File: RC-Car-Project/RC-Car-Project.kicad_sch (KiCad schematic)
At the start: 4 parts

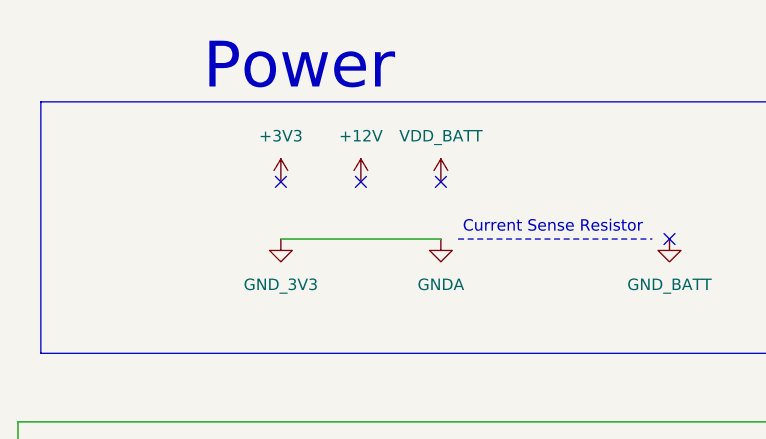
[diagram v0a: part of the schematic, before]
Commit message: Added Camera Connector, Minor Controller Fixes
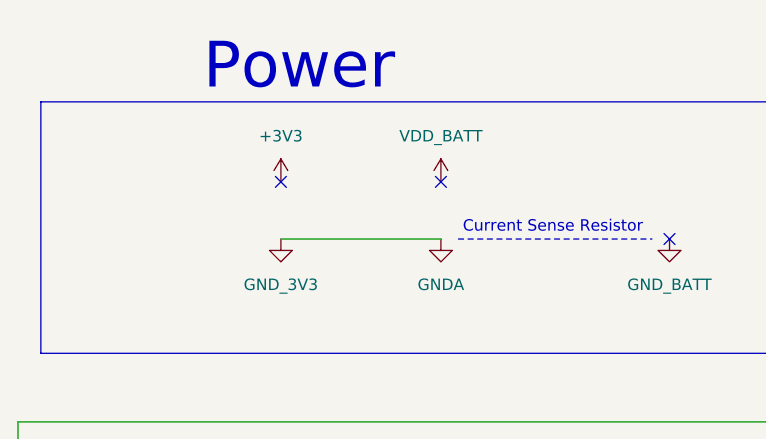
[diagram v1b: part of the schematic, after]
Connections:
- no-connect marks 5 -> 4
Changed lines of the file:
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@@
-	)
-	(no_connect
-		(at 81.28 34.29)
 	)
 	(no_connect
@@
 					(unit 1)
 				)
-			)
-		)
-	)
-	(symbol
-		(lib_id "power:+3V3")
-		(at 81.28 34.29 0)
-		(unit 1)
-		(exclude_from_sim no)
-		(in_bom yes)
-		(on_board yes)
-		(dnp no)
-		(fields_autoplaced yes)
-		(property "Reference" "#PWR012"
-			(at 81.28 38.1 0)
-			(effects
-				(font
-					(size 1.27 1.27)
-				)
-				(hide yes)
-			)
-		)
-		(property "Value" "+12V"
-			(at 81.28 29.21 0)
-			(effects
-				(font
-					(size 1.27 1.27)
-				)
-			)
-		)
-		(property "Footprint" ""
-			(at 81.28 34.29 0)
-			(effects
-				(font
-					(size 1.27 1.27)
-				)
-				(hide yes)
-			)
-		)
-		(property "Datasheet" ""
-			(at 81.28 34.29 0)
-			(effects
-				(font
-					(size 1.27 1.27)
-				)
-				(hide yes)
-			)
-		)
-		(property "Description" "Power symbol creates a global label with name \"+3V3\""
-			(at 81.28 34.29 0)
-			(effects
-				(font
-					(size 1.27 1.27)
-				)
-				(hide yes)
-			)
-		)
-		(pin "1"
-		)
-		(instances
-			(project "RC-Car-Project"
-				(path "/ba870fd1-751d-4755-8e1a-1ea86ca9e2f6"
-					(reference "#PWR012")
-					(unit 1)
-				)

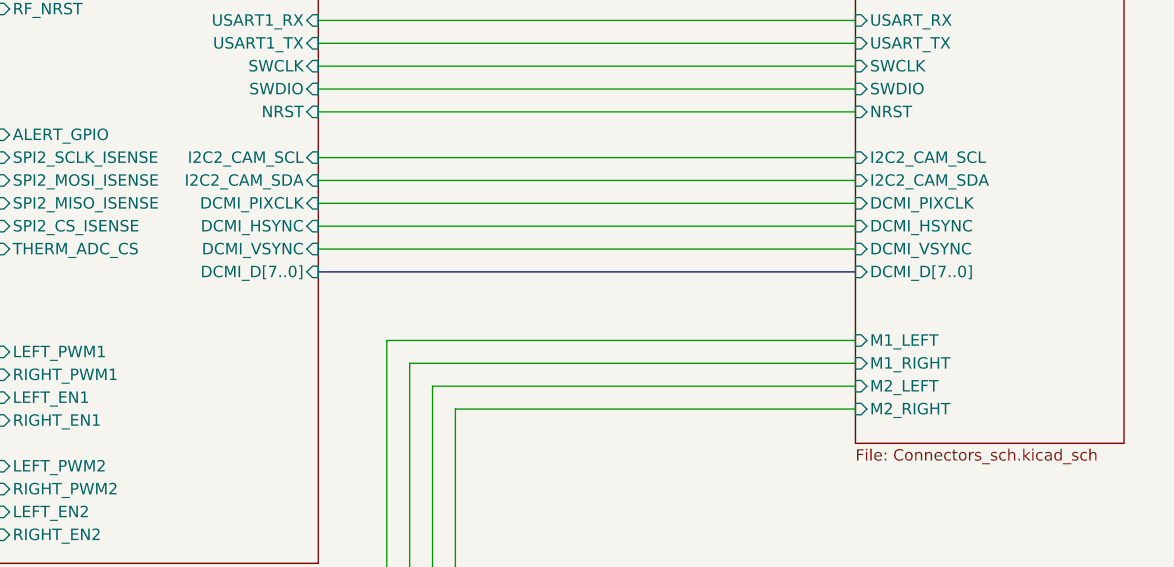
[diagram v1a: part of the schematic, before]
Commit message: Add Camera XCLK
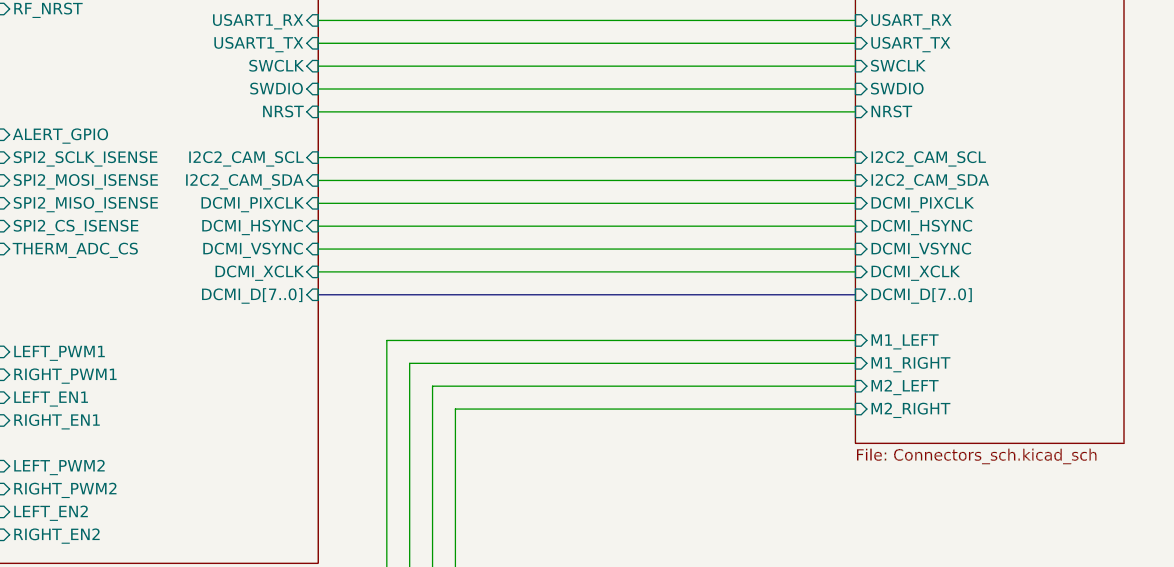
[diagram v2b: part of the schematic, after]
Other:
- sheet Connectors ports: added DCMI_XCLK; removed none
- sheet MCU ports: added DCMI_XCLK; removed none
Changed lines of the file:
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@@
 	(bus
 		(pts
+			(xy 148.59 125.73) (xy 208.28 125.73)
+		)
+		(stroke
+			(width 0)
+			(type default)
+		)
+	)
+	(wire
+		(pts
+			(xy 96.52 83.82) (xy 96.52 88.9)
+		)
+		(stroke
+			(width 0)
+			(type default)
+		)
+	)
+	(wire
+		(pts
+			(xy 204.47 67.31) (xy 204.47 60.96)
+		)
+		(stroke
+			(width 0)
+			(type default)
+		)
+	)
+	(wire
+		(pts
+			(xy 85.09 107.95) (xy 113.03 107.95)
+		)
+		(stroke
+			(width 0)
+			(type default)
+		)
+	)
+	(wire
+		(pts
+			(xy 99.06 86.36) (xy 99.06 81.28)
+		)
+		(stroke
+			(width 0)
+			(type default)
+		)
+	)
+	(wire
+		(pts
+			(xy 85.09 118.11) (xy 113.03 118.11)
+		)
+		(stroke
+			(width 0)
+			(type default)
+		)
+	)
+	(wire
+		(pts
+			(xy 83.82 168.91) (xy 163.83 168.91)
+		)
+		(stroke
+			(width 0)
+			(type default)
+		)
+	)
+	(wire
+		(pts
 			(xy 148.59 123.19) (xy 208.28 123.19)
-		)
-		(stroke
-			(width 0)
-			(type default)
-		)
-	)
-	(wire
-		(pts
-			(xy 96.52 83.82) (xy 96.52 88.9)
-		)
-		(stroke
-			(width 0)
-			(type default)
-		)
-	)
-	(wire
-		(pts
-			(xy 204.47 67.31) (xy 204.47 60.96)
-		)
-		(stroke
-			(width 0)
-			(type default)
-		)
-	)
-	(wire
-		(pts
-			(xy 85.09 107.95) (xy 113.03 107.95)
-		)
-		(stroke
-			(width 0)
-			(type default)
-		)
-	)
-	(wire
-		(pts
-			(xy 99.06 86.36) (xy 99.06 81.28)
-		)
-		(stroke
-			(width 0)
-			(type default)
-		)
-	)
-	(wire
-		(pts
-			(xy 85.09 118.11) (xy 113.03 118.11)
-		)
-		(stroke
-			(width 0)
-			(type default)
-		)
-	)
-	(wire
-		(pts
-			(xy 83.82 168.91) (xy 163.83 168.91)
 		)
 		(stroke
@@
 		)
 		(pin "DCMI_D[7..0]" input
-			(at 208.28 123.19 180)
+			(at 208.28 125.73 180)
 			(effects
 				(font
@@
 		(pin "THERMO2" input
 			(at 208.28 69.85 180)
+			(effects
+				(font
+					(size 1.27 1.27)
+				)
+				(justify left)
+			)
+		)
+		(pin "DCMI_XCLK" input
+			(at 208.28 123.19 180)
 			(effects
 				(font
@@
 		)
 		(pin "DCMI_D[7..0]" input
-			(at 148.59 123.19 0)
+			(at 148.59 125.73 0)
 			(effects
 				(font
@@
 			)
 		)
+		(pin "DCMI_XCLK" input
+			(at 148.59 123.19 0)
+			(effects
+				(font
+					(size 1.27 1.27)
+				)
+				(justify right)
+			)
+		)

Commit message: Fix power
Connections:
- no-connect marks 4 -> 5
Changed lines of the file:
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@@
+	)
+	(no_connect
+		(at 81.28 34.29)
 	)
 	(no_connect
@@
 					(unit 1)
 				)
+			)
+		)
+	)
+	(symbol
+		(lib_id "power:+3V3")
+		(at 81.28 34.29 0)
+		(unit 1)
+		(exclude_from_sim no)
+		(in_bom yes)
+		(on_board yes)
+		(dnp no)
+		(fields_autoplaced yes)
+		(property "Reference" "#PWR0121"
+			(at 81.28 38.1 0)
+			(effects
+				(font
+					(size 1.27 1.27)
+				)
+				(hide yes)
+			)
+		)
+		(property "Value" "+12V"
+			(at 81.28 29.21 0)
+			(effects
+				(font
+					(size 1.27 1.27)
+				)
+			)
+		)
+		(property "Footprint" ""
+			(at 81.28 34.29 0)
+			(effects
+				(font
+					(size 1.27 1.27)
+				)
+				(hide yes)
+			)
+		)
+		(property "Datasheet" ""
+			(at 81.28 34.29 0)
+			(effects
+				(font
+					(size 1.27 1.27)
+				)
+				(hide yes)
+			)
+		)
+		(property "Description" "Power symbol creates a global label with name \"+3V3\""
+			(at 81.28 34.29 0)
+			(effects
+				(font
+					(size 1.27 1.27)
+				)
+				(hide yes)
+			)
+		)
+		(pin "1"
+		)
+		(instances
+			(project "RC-Car-Project"
+				(path "/ba870fd1-751d-4755-8e1a-1ea86ca9e2f6"
+					(reference "#PWR0121")
+					(unit 1)
+				)

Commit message: Fixed Drivers
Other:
- sheet Connectors ports: added LIGHTS1_NEG, LIGHTS1_POS, LIGHTS2_NEG, LIGHTS2_POS; removed LIGHTS_PWM, RELAY_CTRL
- sheet MCU ports: added LIGHTS1_PWM, LIGHTS2_PWM, MOTOR_EN; removed LEFT_EN1, LEFT_EN2, LIGHTS_PWM, RELAY_CTRL, RIGHT_EN1, RIGHT_EN2
- sheet MiscDriver ports: added LIGHTS1_NEG, LIGHTS1_POS, LIGHTS2_NEG, LIGHTS2_POS, MCU_LIGHTS1_CTRL, MCU_LIGHTS2_CTRL; removed LIGHTS_PWM_OUT, MCU_LIGHTS_IN, MCU_RELAY_IN, RELAY_OUT
- sheet MotorDriver ports: added MOTOR_EN; removed MOTOR_1_L_EN, MOTOR_1_R_EN, MOTOR_2_L_EN, MOTOR_2_R_EN

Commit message: Fixed Annotations
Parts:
- D1, D2: footprint LED_SMD:LED_0201_0603Metric -> LED_SMD:LED_0603_1608Metric
- R1: renamed from R13; footprint Resistor_SMD:R_0201_0603Metric -> Resistor_SMD:R_0603_1608Metric
- R2: renamed from R14; footprint Resistor_SMD:R_0201_0603Metric -> Resistor_SMD:R_0603_1608Metric
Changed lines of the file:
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@@
 		(dnp no)
 		(fields_autoplaced yes)
-		(property "Reference" "#PWR081"
+		(property "Reference" "#PWR07"
 			(at 134.62 35.56 0)
 			(effects
@@
 			(project "RC-Car-Project"
 				(path "/ba870fd1-751d-4755-8e1a-1ea86ca9e2f6"
-					(reference "#PWR081")
+					(reference "#PWR07")
 					(unit 1)
 				)
@@
 			)
 		)
-		(property "Footprint" "LED_SMD:LED_0201_0603Metric"
+		(property "Footprint" "LED_SMD:LED_0603_1608Metric"
 			(at 134.62 43.18 0)
 			(effects
@@
 		(dnp no)
 		(fields_autoplaced yes)
-		(property "Reference" "R14"
+		(property "Reference" "R2"
 			(at 171.45 34.2899 0)
 			(effects
@@
 			)
 		)
-		(property "Footprint" "Resistor_SMD:R_0201_0603Metric"
+		(property "Footprint" "Resistor_SMD:R_0603_1608Metric"
 			(at 167.132 35.56 90)
 			(effects
@@
 			(project "RC-Car-Project"
 				(path "/ba870fd1-751d-4755-8e1a-1ea86ca9e2f6"
-					(reference "R14")
+					(reference "R2")
 					(unit 1)
 				)
@@
 		(dnp no)
 		(fields_autoplaced yes)
-		(property "Reference" "#PWR086"
+		(property "Reference" "#PWR010"
 			(at 168.91 53.34 0)
 			(effects
@@
 			(project "RC-Car-Project"
 				(path "/ba870fd1-751d-4755-8e1a-1ea86ca9e2f6"
-					(reference "#PWR086")
+					(reference "#PWR010")
 					(unit 1)
 				)
@@
 		(dnp no)
 		(fields_autoplaced yes)
-		(property "Reference" "#PWR03"
+		(property "Reference" "#PWR04"
 			(at 90.17 38.1 0)
 			(effects
@@
 			(project "RC-Car-Project"
 				(path "/ba870fd1-751d-4755-8e1a-1ea86ca9e2f6"
-					(reference "#PWR03")
+					(reference "#PWR04")
 					(unit 1)
 				)
@@
 		(dnp no)
 		(fields_autoplaced yes)
-		(property "Reference" "R13"
+		(property "Reference" "R1"
 			(at 137.16 34.2899 0)
 			(effects
@@
 			)
 		)
-		(property "Footprint" "Resistor_SMD:R_0201_0603Metric"
+		(property "Footprint" "Resistor_SMD:R_0603_1608Metric"
 			(at 132.842 35.56 90)
 			(effects
@@
 			(project "RC-Car-Project"
 				(path "/ba870fd1-751d-4755-8e1a-1ea86ca9e2f6"
-					(reference "R13")
+					(reference "R1")
 					(unit 1)
 				)
@@
 		(dnp no)
 		(fields_autoplaced yes)
-		(property "Reference" "#PWR085"
+		(property "Reference" "#PWR09"
 			(at 168.91 35.56 0)
 			(effects
@@
 			(project "RC-Car-Project"
 				(path "/ba870fd1-751d-4755-8e1a-1ea86ca9e2f6"
-					(reference "#PWR085")
+					(reference "#PWR09")
 					(unit 1)
 				)
@@
 		(dnp no)
 		(fields_autoplaced yes)
-		(property "Reference" "#PWR0121"
+		(property "Reference" "#PWR03"
 			(at 81.28 38.1 0)
 			(effects
@@
 			(project "RC-Car-Project"
 				(path "/ba870fd1-751d-4755-8e1a-1ea86ca9e2f6"
-					(reference "#PWR0121")
+					(reference "#PWR03")
 					(unit 1)
 				)
@@
 		(dnp no)
 		(fields_autoplaced yes)
-		(property "Reference" "#PWR082"
+		(property "Reference" "#PWR08"
 			(at 134.62 53.34 0)
 			(effects
@@
 			(project "RC-Car-Project"
 				(path "/ba870fd1-751d-4755-8e1a-1ea86ca9e2f6"
-					(reference "#PWR082")
+					(reference "#PWR08")
 					(unit 1)
 				)
@@
 		(dnp no)
 		(fields_autoplaced yes)
-		(property "Reference" "#PWR04"
+		(property "Reference" "#PWR06"
 			(at 115.57 46.99 0)
 			(effects
@@
 			(project "RC-Car-Project"
 				(path "/ba870fd1-751d-4755-8e1a-1ea86ca9e2f6"
-					(reference "#PWR04")
+					(reference "#PWR06")
 					(unit 1)
 				)
@@
 			)
 		)
-		(property "Footprint" "LED_SMD:LED_0201_0603Metric"
+		(property "Footprint" "LED_SMD:LED_0603_1608Metric"
 			(at 168.91 43.18 0)
 			(effects
@@
 		(dnp no)
 		(fields_autoplaced yes)
-		(property "Reference" "#PWR07"
+		(property "Reference" "#PWR05"
 			(at 90.17 46.99 0)
 			(effects
@@
 			(project ""
 				(path "/ba870fd1-751d-4755-8e1a-1ea86ca9e2f6"
-					(reference "#PWR07")
+					(reference "#PWR05")
 					(unit 1)
 				)
@@
 		(dnp no)
 		(fields_autoplaced yes)
-		(property "Reference" "#PWR02"
+		(property "Reference" "#PWR01"
 			(at 72.39 38.1 0)
 			(effects
@@
 			(project ""
 				(path "/ba870fd1-751d-4755-8e1a-1ea86ca9e2f6"
-					(reference "#PWR02")
+					(reference "#PWR01")
 					(unit 1)
 				)
@@
 		(dnp no)
 		(fields_autoplaced yes)
-		(property "Reference" "#PWR01"
+		(property "Reference" "#PWR02"
 			(at 72.39 46.99 0)
 			(effects
@@
 			(project ""
 				(path "/ba870fd1-751d-4755-8e1a-1ea86ca9e2f6"
-					(reference "#PWR01")
-					(unit 1)
-				)
+					(reference "#PWR02")
+					(unit 1)
+				)

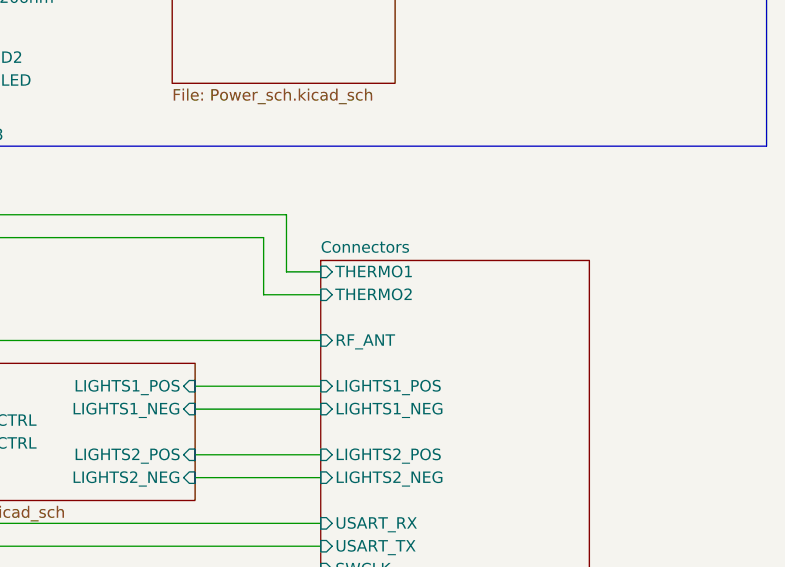
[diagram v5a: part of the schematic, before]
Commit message: Add RF filter + another thermo header + layout everything
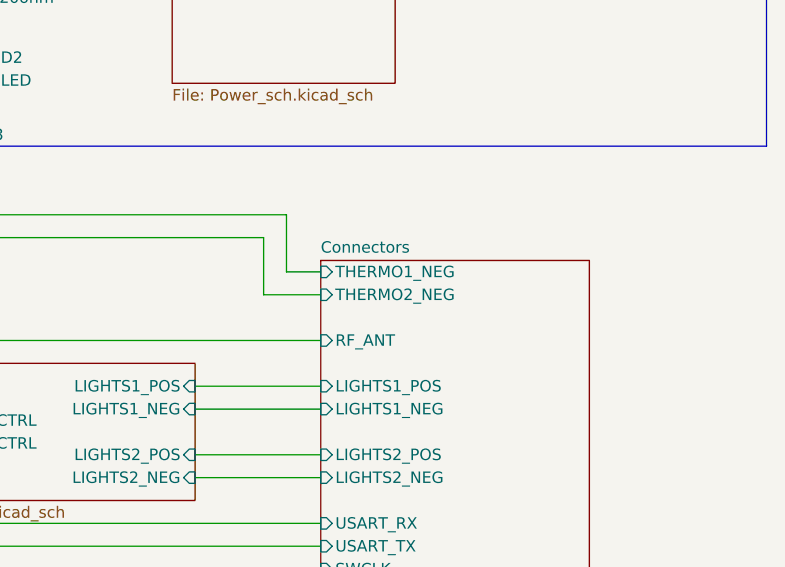
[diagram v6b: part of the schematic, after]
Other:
- sheet Connectors ports: added THERMO1_NEG, THERMO2_NEG; removed THERMO1, THERMO2
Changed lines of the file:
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@@
-			)
-		)
-		(pin "THERMO1" input
-			(at 208.28 67.31 180)
-			(effects
-				(font
-					(size 1.27 1.27)
-				)
-				(justify left)
-			)
-		)
-		(pin "THERMO2" input
-			(at 208.28 69.85 180)
-			(effects
-				(font
-					(size 1.27 1.27)
-				)
-				(justify left)
 			)
 		)
@@
 			(effects
 				(font
+					(size 1.27 1.27)
+				)
+				(justify left)
+			)
+		)
+		(pin "THERMO1_NEG" input
+			(at 208.28 67.31 180)
+			(effects
+				(font
+					(size 1.27 1.27)
+				)
+				(justify left)
+			)
+		)
+		(pin "THERMO2_NEG" input
+			(at 208.28 69.85 180)
+			(effects
+				(font
